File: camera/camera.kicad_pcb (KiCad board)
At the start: 2 copper layers, 32.5 x 32.5 mm, 68 parts, among them J1 Gecko, J2 USB_B_Micro, J3 Programmer, J4 OV5640, J5 Micro_SD_Card, U1 INA180, U2 TPS562200, U3 MCP2562, U4 STM32H750VBTx, U5 TLV70215_SOT23-5, U6 AP2171W, X1 ECS-2520MV-240-BN

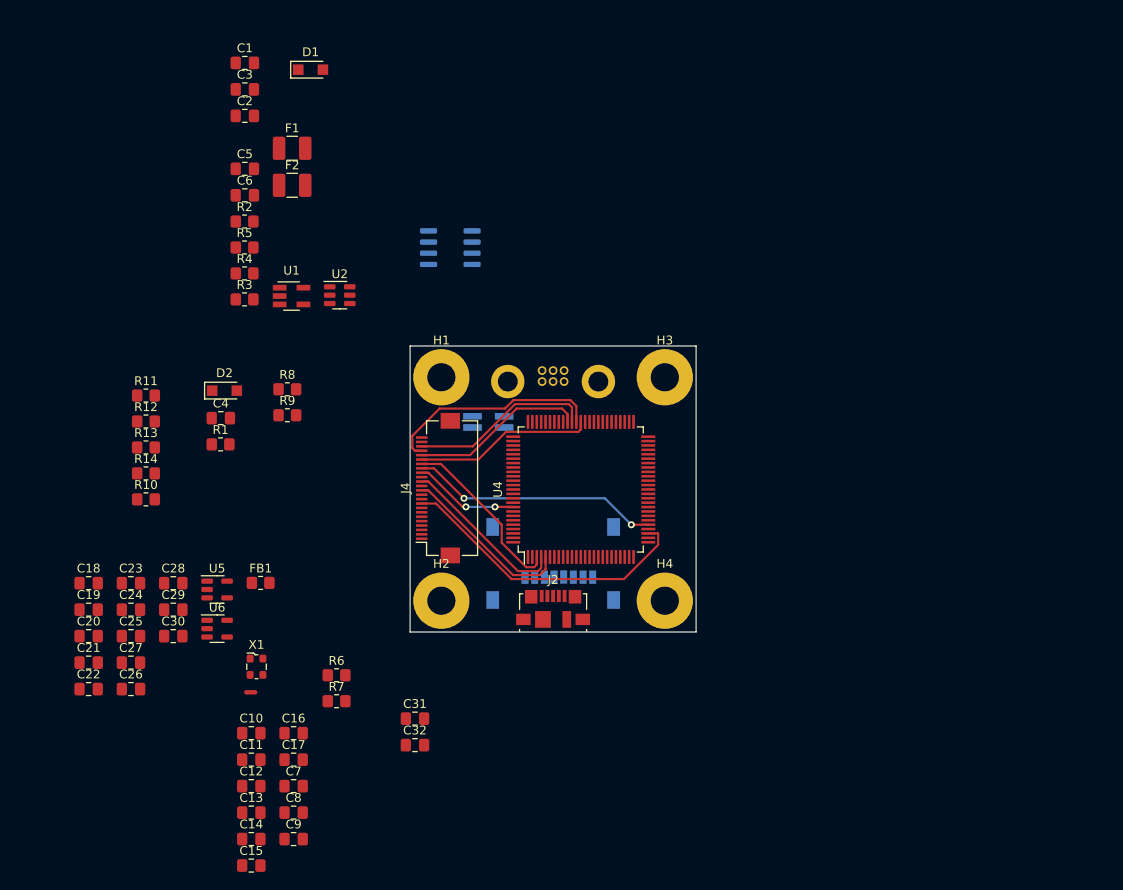
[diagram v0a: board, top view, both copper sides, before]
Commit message: Add testpoint and clean up schematic, layout WIP
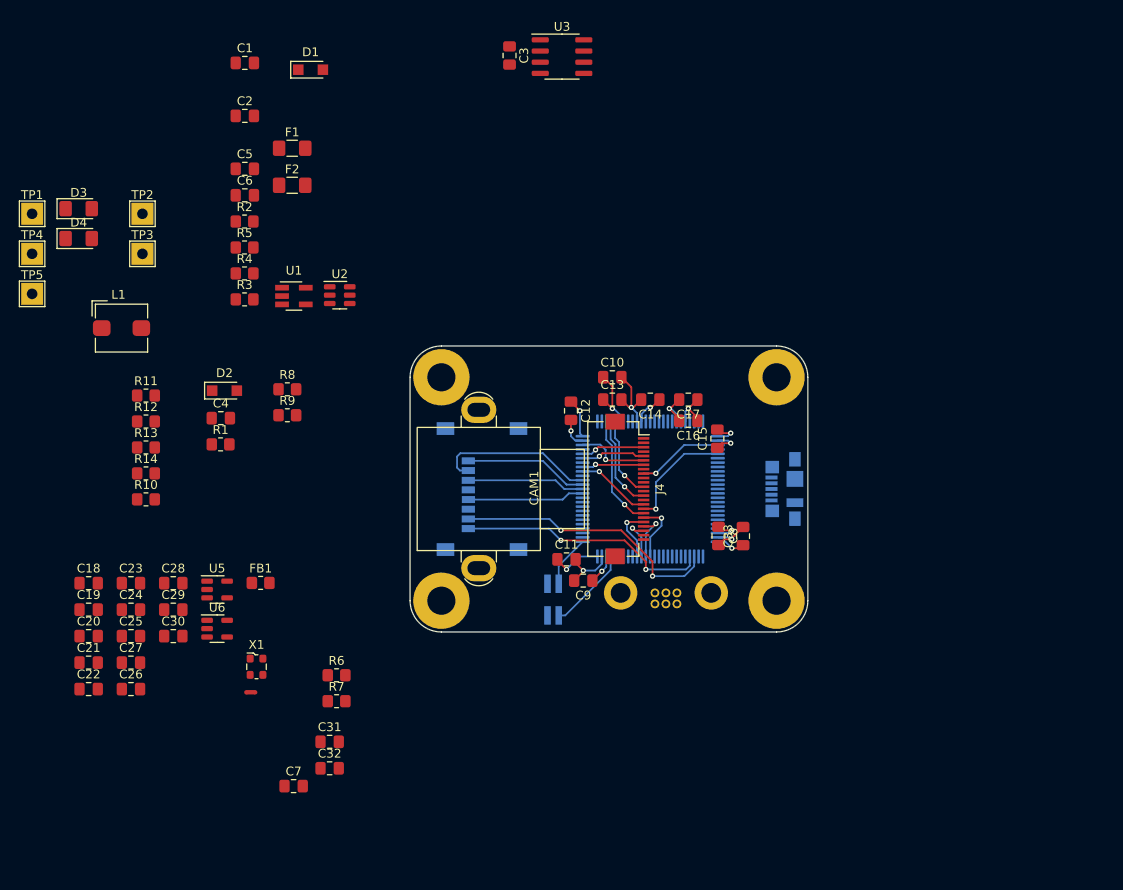
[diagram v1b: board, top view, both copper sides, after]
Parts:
- added C33: 100n, Capacitor_SMD:C_0805_2012Metric_Pad1.18x1.45mm_HandSolder, F.Cu at (193.8, 105.4)
- added CAM1: OV5640, canhw_footprints:OV5640, F.Cu at (175.8, 100.1)
- added D3: RED, LED_SMD:LED_1206_3216Metric_Pad1.42x1.75mm_HandSolder, F.Cu at (118.3, 68.2)
- added D4: GREEN, LED_SMD:LED_1206_3216Metric_Pad1.42x1.75mm_HandSolder, F.Cu at (118.3, 71.6)
- added L1: SRP5030T-3R3M, Inductor_SMD:L_Bourns_SRP5030T, F.Cu at (123.2, 81.8)
- added TP1: NRST, TestPoint:TestPoint_THTPad_2.5x2.5mm_Drill1.2mm, F.Cu at (113.0, 68.8)
- added TP2: XCLK, TestPoint:TestPoint_THTPad_2.5x2.5mm_Drill1.2mm, F.Cu at (125.5, 68.8)
- added TP3: PIXCLK, TestPoint:TestPoint_THTPad_2.5x2.5mm_Drill1.2mm, F.Cu at (125.5, 73.3)
- added TP4: SCL, TestPoint:TestPoint_THTPad_2.5x2.5mm_Drill1.2mm, F.Cu at (113.0, 73.3)
- added TP5: SDA, TestPoint:TestPoint_THTPad_2.5x2.5mm_Drill1.2mm, F.Cu at (113.0, 77.9)
- F1, F2: footprint Fuse:Fuse_1210_3225Metric_Pad1.42x2.65mm_HandSolder -> Fuse:Fuse_1206_3216Metric_Pad1.42x1.75mm_HandSolder
- J2, U4: moved to B.Cu
- U3: moved to F.Cu
- moved C15 71.8 mm to (190.9, 94.4), turned to 90 degrees
- moved C14 67.5 mm to (183.3, 89.9), turned to 180 degrees
- moved C13 62.4 mm to (178.9, 89.9)
- moved C17 60.7 mm to (187.6, 89.9), turned to 180 degrees
- moved C8 57.6 mm to (191.0, 105.4), turned to -90 degrees
- moved C10 57.6 mm to (178.9, 87.4)
- moved C16 57.2 mm to (187.6, 92.3), turned to 180 degrees
- moved C12 56.0 mm to (174.2, 91.2), turned to -90 degrees
- moved C9 44.1 mm to (175.6, 110.5), turned to 180 degrees
- moved C11 42.4 mm to (173.7, 108.1)
- moved C3 30.3 mm to (167.3, 50.8), turned to 90 degrees
- moved J2 29.6 mm to (198.5, 100.1), turned to -90 degrees
- moved J1 27.2 mm to (185.0, 111.9), turned to 180 degrees
- moved U3 25.2 mm to (173.2, 50.9), turned to 0 degrees
- moved J4 21.5 mm to (180.7, 100.1), turned to -90 degrees
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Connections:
- C9 pad 1: Net-(C8-Pad1) -> Net-(C9-Pad1)
- U4 pad 73: Net-(C8-Pad1) -> Net-(C9-Pad1)
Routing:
- net +2V8: track 0.00 -> 32.7 mm, vias 0 -> 7
- net GND: track 0.00 -> 32.7 mm, vias 0 -> 6
- net /MCU/SD_D0: track 0.00 -> 30.9 mm, vias 0 -> 2
- net /MCU/SD_D1: track 0.00 -> 28.8 mm, vias 0 -> 2
- net /MCU/HSYNC: track 34.4 -> 9.77 mm, vias 0 -> 1
- net /MCU/DCMI_D1: track 25.0 -> 5.74 mm, vias 0 -> 1
- net /MCU/SD_D3: track 0.00 -> 18.4 mm
- net /MCU/DCMI_D2: track 20.9 -> 5.05 mm, vias 0 -> 1
- net /MCU/PIXCLK: track 28.4 -> 12.8 mm, vias 2 -> 1
- net /MCU/SD_D2: track 0.00 -> 14.1 mm
- net /MCU/DCMI_D3: track 19.9 -> 6.27 mm, vias 0 -> 1
- net /MCU/SD_CMD: track 0.00 -> 13.4 mm
- net /MCU/DCMI_D0: track 20.4 -> 6.96 mm, vias 0 -> 1
- net /MCU/SD_CLK: track 0.00 -> 13.3 mm
- net /MCU/DCMI_D7: track 19.7 -> 9.29 mm, vias 0 -> 1
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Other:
- board size 32.5 x 32.5 mm -> 45.2 x 32.5 mm

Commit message: Complete layout along with high-speed routing
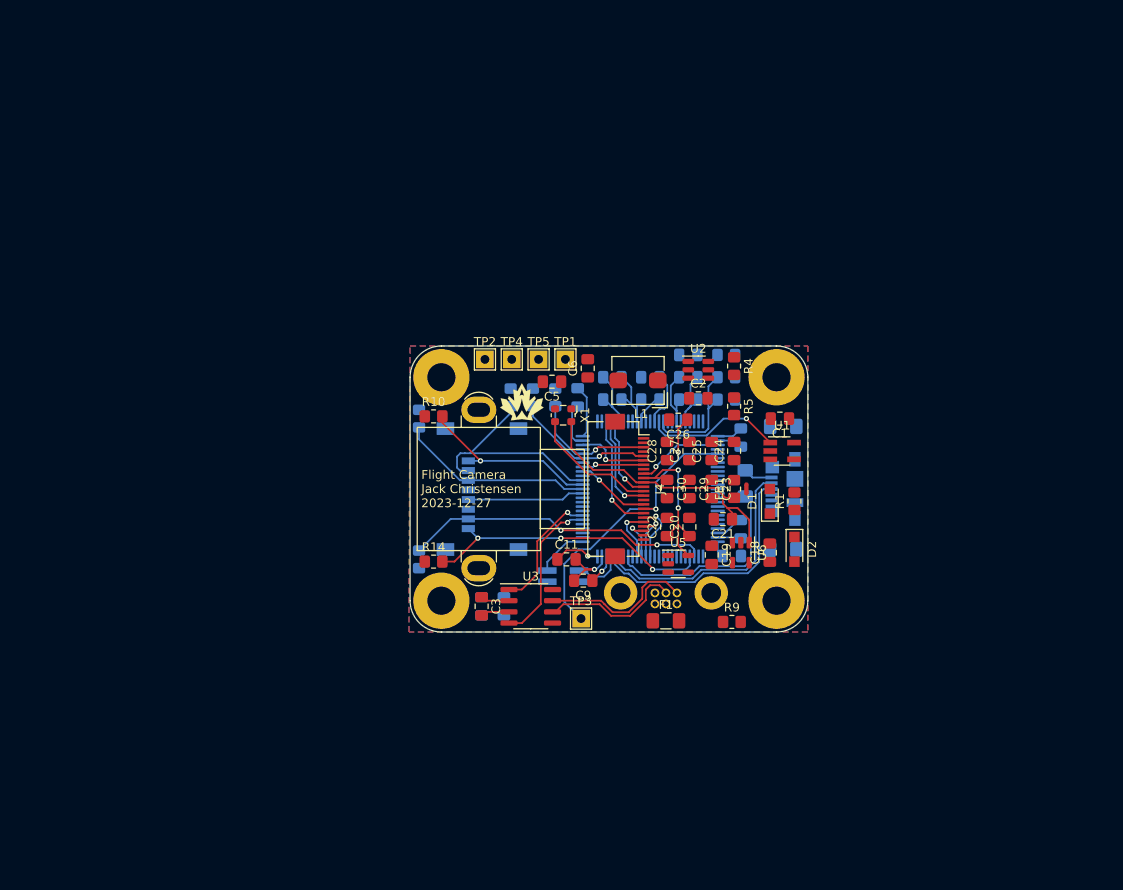
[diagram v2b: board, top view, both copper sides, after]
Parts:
- added G***: LOGO, Team_Logo:Logo_SilkScreen_5mm, F.Cu at (168.7, 90.2)
- C10, C12, C13, C14, C15, C16, C17, C31, C32, C33, C4, C7, C8, D3, D4, F2, R11, R12, R13, R2, R3, R6, R7, R8: moved to B.Cu
- TP1, TP2, TP3, TP4, TP5: footprint TestPoint:TestPoint_THTPad_2.5x2.5mm_Drill1.2mm -> TestPoint:TestPoint_THTPad_2.0x2.0mm_Drill1.0mm
- moved D4 87.5 mm to (198.4, 106.9), turned to 180 degrees
- moved D3 83.8 mm to (198.4, 93.0), turned to 180 degrees
- moved C18 77.5 mm to (196.8, 107.3), turned to 90 degrees
- moved C21 73.9 mm to (191.5, 103.5), turned to 180 degrees
- moved C1 73.0 mm to (198.0, 92.1), turned to 180 degrees
- moved D1 71.6 mm to (196.8, 101.5), turned to 90 degrees
- moved C19 71.1 mm to (190.2, 107.6), turned to -90 degrees
- moved C24 70.9 mm to (192.8, 95.8), turned to 90 degrees
- moved C20 69.4 mm to (187.7, 104.4), turned to 90 degrees
- moved C26 69.3 mm to (186.4, 92.2), turned to 180 degrees
- moved C25 69.3 mm to (190.2, 95.8), turned to 90 degrees
- moved F1 68.5 mm to (185.0, 115.1)
- moved C22 68.3 mm to (185.2, 104.4), turned to 90 degrees
- moved C27 67.9 mm to (187.7, 95.8), turned to 90 degrees
- moved D2 67.3 mm to (199.6, 106.9), turned to -90 degrees
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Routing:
- net /OV5640/DOVDD: track 0.00 -> 35.2 mm
- net /USB_D+: track 0.00 -> 28.5 mm
- net /USB_D-: track 0.00 -> 27.9 mm
- net /MCU/PIXCLK: track 12.8 -> 37.8 mm, vias 1 -> 2
- net /VBUS: track 0.00 -> 23.5 mm
- net /OV5640/DVDD: track 0.00 -> 19.6 mm, vias 0 -> 2
- net /CANH: track 0.00 -> 17.4 mm
- net /CAN_RX: track 0.00 -> 17.3 mm, vias 0 -> 1
- net /CANL: track 0.00 -> 16.4 mm
- net /CURR_SENS: track 0.00 -> 15.8 mm, vias 0 -> 1
- net /OV5640/XCLK: track 0.00 -> 14.7 mm
- net /CAN_TX: track 0.00 -> 14.3 mm, vias 0 -> 1
- net /V_SENS: track 0.00 -> 14.0 mm
- net /MCU/SD_CMD: track 13.4 -> 22.3 mm
- net /MCU/SCL: track 7.29 -> 16.1 mm
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- added copper zone on In1.Cu, net +2V8
- added copper zone on B.Cu, net GND
- added copper zone on F.Cu, net GND
- added copper zone on In2.Cu, net GND
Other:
- copper layers 2 -> 4
- board text added: "Flight Camera Jack Christensen 2023-12-27"

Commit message: Complete routing, ready for review
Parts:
- TP1, TP2, TP3, TP4, TP5: moved to B.Cu
- moved NT1 7.12 mm to (191.5, 93.5), turned to 180 degrees
- moved J3 0.76 mm to (172.6, 110.0)
- turned C26 to 0 degrees
- turned TP1 to 180 degrees
- turned TP2 to 180 degrees
- turned TP3 to 180 degrees
- turned TP4 to 180 degrees
- turned TP5 to 180 degrees
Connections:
- U4 pad 47: unconnected-(U4-PB11-Pad47) -> /MCU/CAM_EN
- U4 pad 97: /MCU/CAM_EN -> unconnected-(U4-PE0-Pad97)
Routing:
- net GND: track 38.3 -> 129.1 mm, vias 1 -> 32
- net +2V8: track 33.9 -> 87.5 mm, vias 1 -> 24
- net VDC: track 0.00 -> 42.5 mm, vias 0 -> 1
- net /MCU/LED_G: track 0.00 -> 22.4 mm, vias 0 -> 1
- net /OV5640/AVDD: track 0.00 -> 19.1 mm
- net +5V: track 3.28 -> 22.3 mm, vias 0 -> 1
- net /MCU/LED_R: track 0.00 -> 18.9 mm
- net Net-(D2-A): track 0.00 -> 17.6 mm, vias 0 -> 2
- net Net-(D1-K): track 0.00 -> 17.2 mm
- net GNDA: track 0.00 -> 16.8 mm
- net /MCU/CAM_EN: track 0.00 -> 15.5 mm, vias 0 -> 1
- net Net-(U4-NRST): track 6.28 -> 20.2 mm
- net /OV5640/XCLK: track 14.7 -> 27.2 mm
- net Net-(D3-A): track 0.00 -> 9.78 mm
- net Net-(D4-A): track 0.00 -> 9.64 mm, vias 0 -> 1
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- added copper zone on F.Cu, net +2V8
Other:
- board text added: "Flight Camera Jack Christensen 2023-12-30"
- board text removed: "Flight Camera Jack Christensen 2023-12-27"

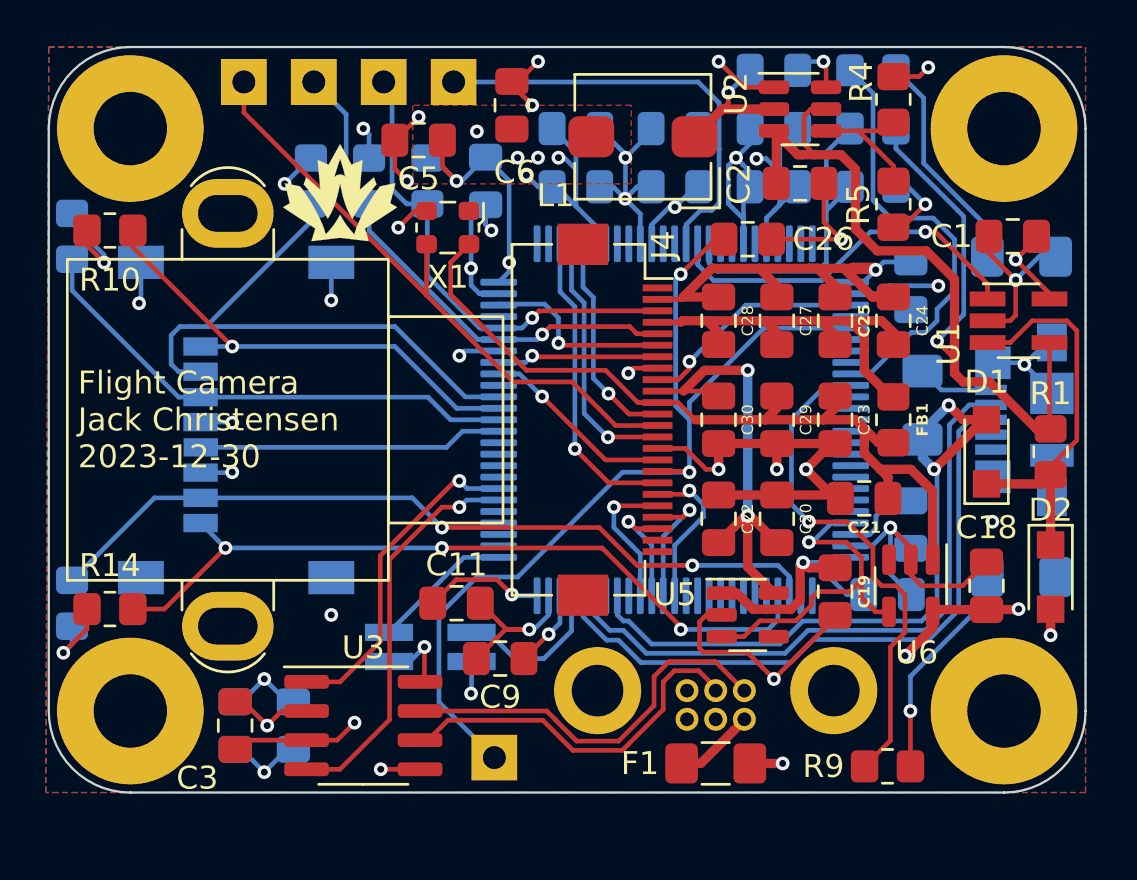
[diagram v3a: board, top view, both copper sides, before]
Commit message: Camera board mirrored connector (#85)
* Fix flipped camera connector, and minor tweaks

* Add programming silkscreen

* Generated gerbers
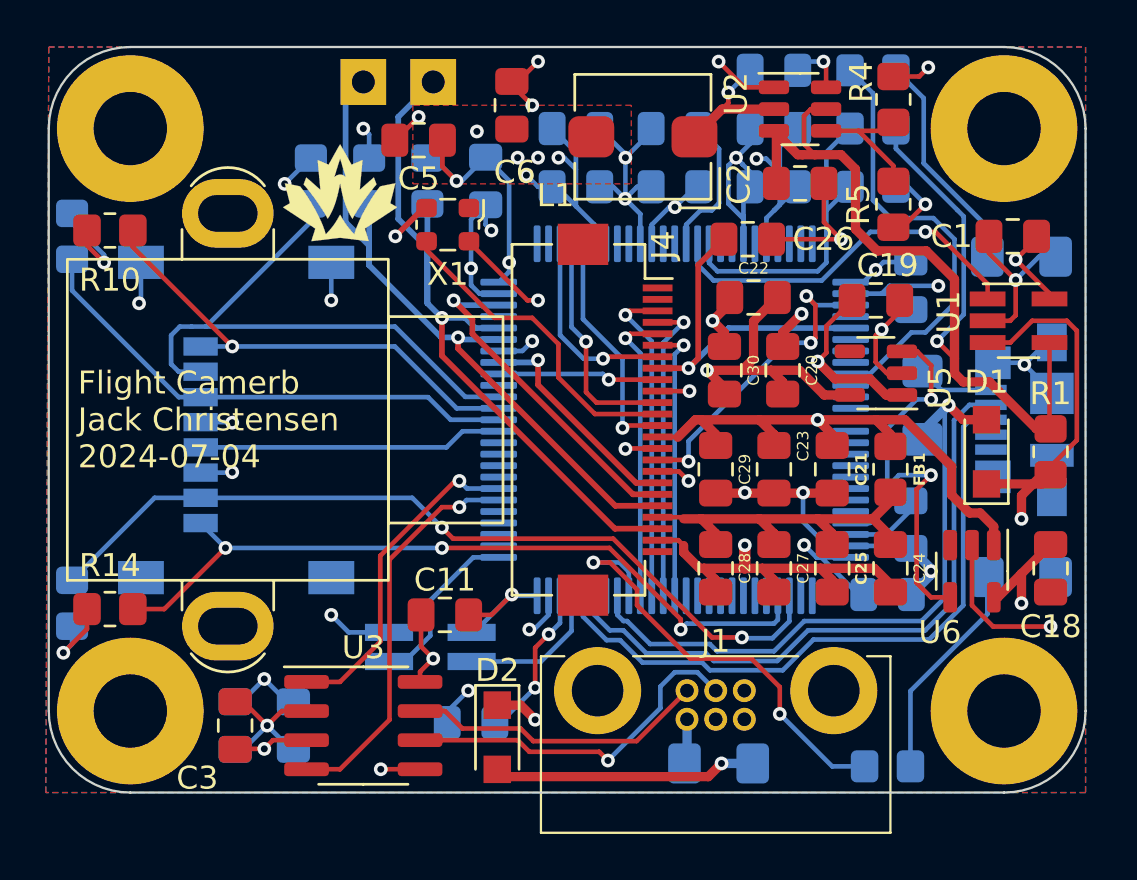
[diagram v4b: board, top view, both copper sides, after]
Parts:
- removed TP1: NRST, TestPoint:TestPoint_THTPad_2.0x2.0mm_Drill1.0mm
- removed TP2: XCLK, TestPoint:TestPoint_THTPad_2.0x2.0mm_Drill1.0mm
- removed TP3: PIXCLK, TestPoint:TestPoint_THTPad_2.0x2.0mm_Drill1.0mm
- C9, F1, R9: moved to B.Cu
- J1: moved to F.Cu
- moved D2 25.1 mm to (175.5, 113.9)
- moved NT1 13.6 mm to (186.3, 106.0), turned to -90 degrees
- moved C19 12.8 mm to (192.0, 94.9), turned to 0 degrees
- moved U5 11.9 mm to (192.0, 98.0), turned to 180 degrees
- moved C24 10.8 mm to (192.7, 106.6), turned to -90 degrees
- moved C25 10.8 mm to (190.1, 106.6), turned to -90 degrees
- moved C27 10.8 mm to (187.6, 106.6), turned to -90 degrees
- moved C28 10.8 mm to (185.0, 106.6), turned to -90 degrees
- moved C22 9.77 mm to (186.7, 94.7), turned to 180 degrees
- moved C20 6.48 mm to (188.0, 97.9)
- moved C23 3.43 mm to (187.6, 102.2)
- moved C29 3.43 mm to (185.0, 102.2)
- moved C9 3.07 mm to (174.4, 113.3)
- moved C18 2.90 mm to (199.6, 106.6), turned to -90 degrees
- moved U6 2.74 mm to (196.2, 106.7)
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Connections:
- J3 pad 1: +2V8 -> GND
- J3 pad 2: GND -> +2V8
- J3 pad 3: /MCU/SWDIO -> /MCU/SWCLK
- J3 pad 4: /MCU/SWCLK -> /MCU/SWDIO
- J4 pad 10: /OV5640/DVDD -> GND
- J4 pad 11: /OV5640/DOVDD -> /MCU/DCMI_D6
- J4 pad 12: /MCU/DCMI_D7 -> /OV5640/XCLK
- J4 pad 13: /OV5640/XCLK -> /MCU/DCMI_D7
- J4 pad 14: /MCU/DCMI_D6 -> /OV5640/DOVDD
- J4 pad 15: GND -> /OV5640/DVDD
- J4 pad 16: /MCU/DCMI_D5 -> /MCU/HSYNC
- J4 pad 17: /MCU/PIXCLK -> GND
- J4 pad 18: /MCU/DCMI_D4 -> /MCU/VSYNC
- J4 pad 19: /MCU/DCMI_D0 -> /MCU/CAM_~{RESET}
- J4 pad 2: GNDA -> unconnected-(J4-Pin_2-Pad2)
- J4 pad 20: /MCU/DCMI_D3 -> /MCU/SCL
- J4 pad 21: /MCU/DCMI_D1 -> /OV5640/AVDD
- J4 pad 22: /MCU/DCMI_D2 -> /MCU/SDA
- J4 pad 23: unconnected-(J4-Pin_23-Pad23) -> GNDA
- J4 pad 3: /MCU/SDA -> /MCU/DCMI_D2
- J4 pad 4: /OV5640/AVDD -> /MCU/DCMI_D1
- J4 pad 5: /MCU/SCL -> /MCU/DCMI_D3
- J4 pad 6: /MCU/CAM_~{RESET} -> /MCU/DCMI_D0
- J4 pad 7: /MCU/VSYNC -> /MCU/DCMI_D4
- J4 pad 8: GND -> /MCU/PIXCLK
- J4 pad 9: /MCU/HSYNC -> /MCU/DCMI_D5
- U4 pad 35: /MCU/LED_G -> unconnected-(U4-PB1-Pad35)
- U4 pad 67: unconnected-(U4-PA8-Pad67) -> /MCU/LED_G
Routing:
- net Net-(D1-K): track 17.2 -> 47.7 mm, vias 0 -> 2
- net /MCU/PIXCLK: track 42.8 -> 15.4 mm, vias 2 -> 1
- net Net-(U4-NRST): track 20.2 -> 6.28 mm
- net GND: track 129.1 -> 115.4 mm, vias 32 -> 34
- net /OV5640/XCLK: track 27.2 -> 14.3 mm
- net /MCU/SDA: track 21.1 -> 32.9 mm
- net /MCU/DCMI_D2: track 5.05 -> 14.2 mm
- net /MCU/SCL: track 22.4 -> 30.4 mm
- net /MCU/DCMI_D1: track 5.74 -> 13.4 mm
- net /OV5640/DOVDD: track 36.2 -> 42.9 mm, vias 0 -> 2
- net /MCU/DCMI_D3: track 6.27 -> 13.0 mm
- net /MCU/CAM_~{RESET}: track 8.34 -> 14.8 mm
- net Net-(D2-A): track 17.6 -> 11.5 mm, vias 2 -> 1
- net /MCU/DCMI_D0: track 6.82 -> 12.2 mm
- net /MCU/DCMI_D4: track 13.4 -> 8.70 mm
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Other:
- board text added: "Flight Camerb Jack Christensen 2024-07-04"
- board text removed: "Flight Camera Jack Christensen 2023-12-30"
